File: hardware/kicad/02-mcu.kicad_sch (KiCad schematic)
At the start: 6 parts, among them SW14 BOOT, SW15 RESET, U1 ESP32-S3-N16R8

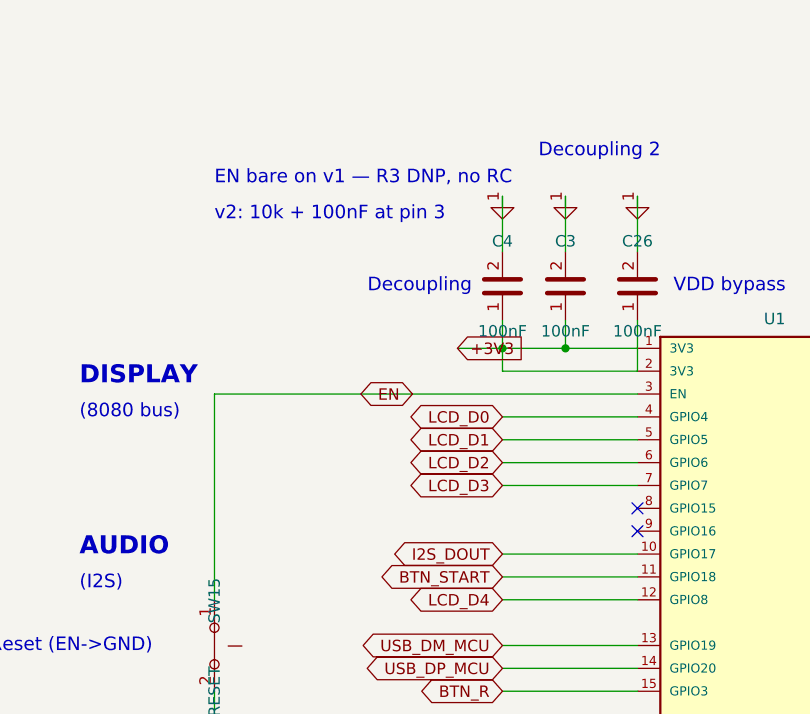
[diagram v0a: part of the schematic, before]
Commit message: feat(hw): EN RC network, fused VBUS input, current-limited backlight — R25 respin trio
Three coordinated design fixes landed together with their full gate,
bench and release integration (work split across two parallel sessions):

- R3 (10k) + C31 (100nF) on EN — the RC the module datasheet p.28
  fig.7 requires (R25-CRIT-1: every board through v4.3.1 shipped
  without it on the strength of a false justification comment).
  EN now solves to the +3V3 rail through the pull-up.
- F1 (PTC resettable fuse 2A 1812, C960026) on the USB input:
  J1 delivers on the new VBUS_IN net and reaches VBUS through F1.
  PWR_FLAG added on the post-fuse rail (J1's power-out pin moved nets).
- R27 (20R 1206) backlight series resistor: LED-A now fed from +5V
  through R27 on the new LED_BLA net (R25-HIGH-1, unbounded current).
  First placement collided with the LCD B.Cu verticals; final position
  (121.7, 45.5) clears the corridor.

Integration completed in this commit:
- verify_polarity: strict expectations for R3/C31/R27/F1, J1 pins moved
  to VBUS_IN, J4.8 backlight expectation moved to LED_BLA — all read
  off the copper.
- vbench corpus: R25-CRIT-1, R10-LOW-7, R25-HIGH-1 flipped from live
  board facts to mutation reinjection (detach R3/C31/R27 must be caught
  by name); R24-HIGH-3 moved to a move_pin drift mutation — the detach
  variant became structurally invisible to the bench once EN gained
  R3/C31 (declared-pad D3 exemption); note records why. usb_cold_boot
  flips its EN assertion exactly as its own text promised; export
  header now derives VB_EN_FLOATING=0; VBUS invariant follows the
  fused chain.
- Gates: R_1206/F_1812 footprints known, F1 value mapping, LED_BLA in
  the Net Explorer section law, schematic caption collisions resolved.
- Release fully synced (gerbers, BOM, CPL, d356, zip, jlcpcb mirror),
  iBOM + schematic SVG/PDF renders + combined PDF regenerated.

Tests: verify-all ALL CHECKS PASSED (incl. polarity 274 checks,
netlist-diff, isolation, e-test on release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
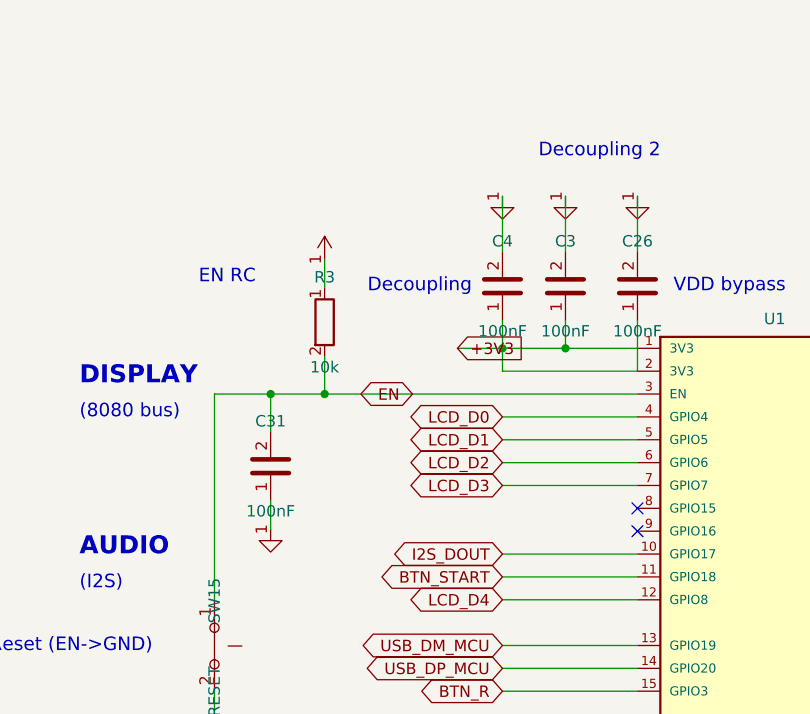
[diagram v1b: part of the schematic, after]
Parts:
- added C26, C3: 100nF, symbol C
- C31: renamed from SW14; value BOOT -> 100nF; symbol SW_Push -> C
- R3: renamed from SW15; value RESET -> 10k; symbol SW_Push -> R
- SW14: renamed from C3; value 100nF -> BOOT; symbol C -> SW_Push
- SW15: renamed from C4; value 100nF -> RESET; symbol C -> SW_Push
- renumbered C26 to C4
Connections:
- net +3V3: now also R3.1, C26.1, C3.1; no longer SW14.1, SW15.1
- net BTN_SELECT: now also SW14.1; no longer C31.1
- net EN: now also C31.2, R3.2, SW15.1; no longer R3.1
- net GND: now also C31.1, C26.2, C3.2; no longer C31.2, R3.2
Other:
- note added: "EN RC"
- note removed: "EN bare on v1 — R3 DNP, no RC"
- note removed: "v2: 10k + 100nF at pin 3"
- moved on the sheet: C4

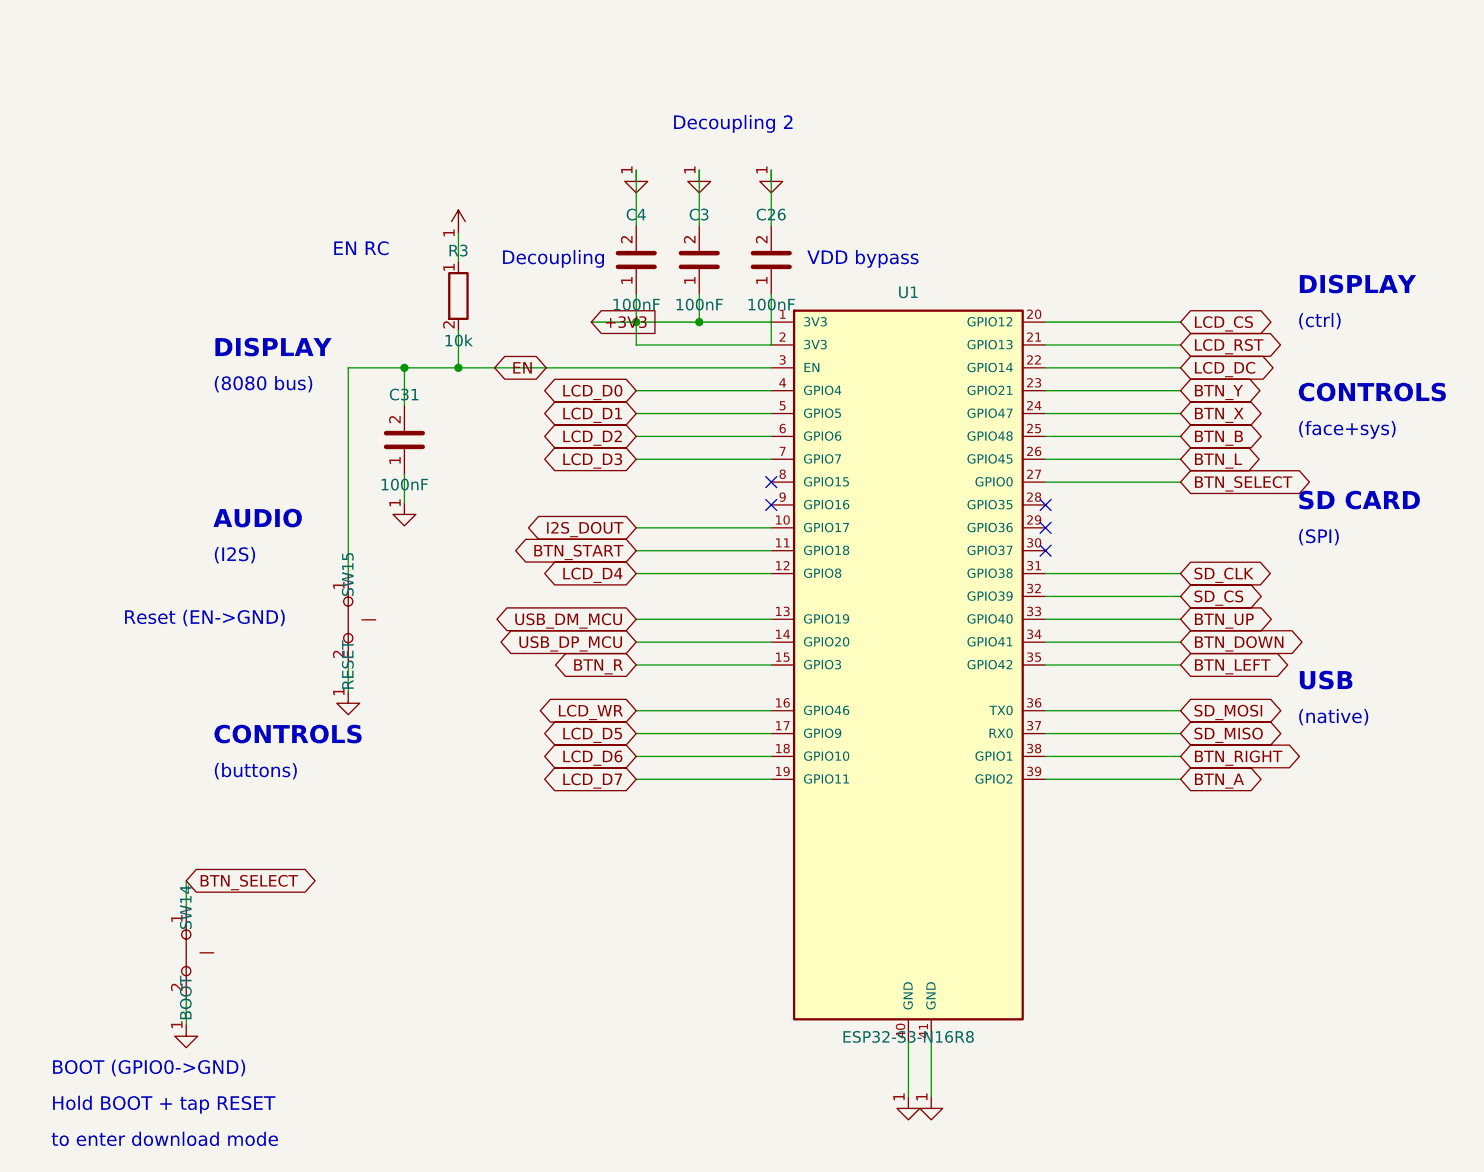
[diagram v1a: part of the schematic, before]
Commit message: feat(containment): layer 6 — ERC warning burn-down, 676 to ZERO, gate at all severities
Three root causes, three fixes in the schematic generator:

- 507 endpoint_off_grid: sheets lay out on a human 1 mm grid while KiCad
  connects on 1.27 mm. snap() in kicad_primitives now grid-snaps every
  connection-bearing coordinate at emission. Snapping is monotonic and
  distributes over the library's grid-multiple pin offsets, so points
  that coincided before still coincide after; zero-length stub wires
  that collapse onto their anchor are dropped.
- The stragglers came from three symbols whose pin connection points
  were themselves off-grid: BAT54C (±5.0 → ±5.08, top 5.0 → 5.08, used
  by D1 and Q1), USBLC6-2SC6 (±10.0 → ±10.16), Speaker (±0.635 →
  ±1.27). Their sheet wiring moved with them in the same commit.
- 169 lib_symbol_issues: bare lib_ids referenced library "" which no
  configuration includes. Symbols are now emu:<name>, resolved by a
  generated hardware/kicad/sym-lib-table + emu.kicad_sym built from the
  same SYMBOLS strings as the embedded caches — cache and library
  cannot disagree by construction.

verify_erc now runs --severity-all against a ZERO baseline: from zero,
any new warning is a regression a specific change introduced. The
website's per-sheet SVGs/PDFs are re-rendered, and the "Download all
sheets" PDF — a one-off hand merge nothing regenerated, stale since the
R25 respin — is now merged by render-schematics.sh from the exported
sheets.

Suite: 85/85 green; netlist_diff vs PCB confirms connectivity unchanged.

Co-Authored-By: Claude Fable 5 <noreply@anthropic.com>
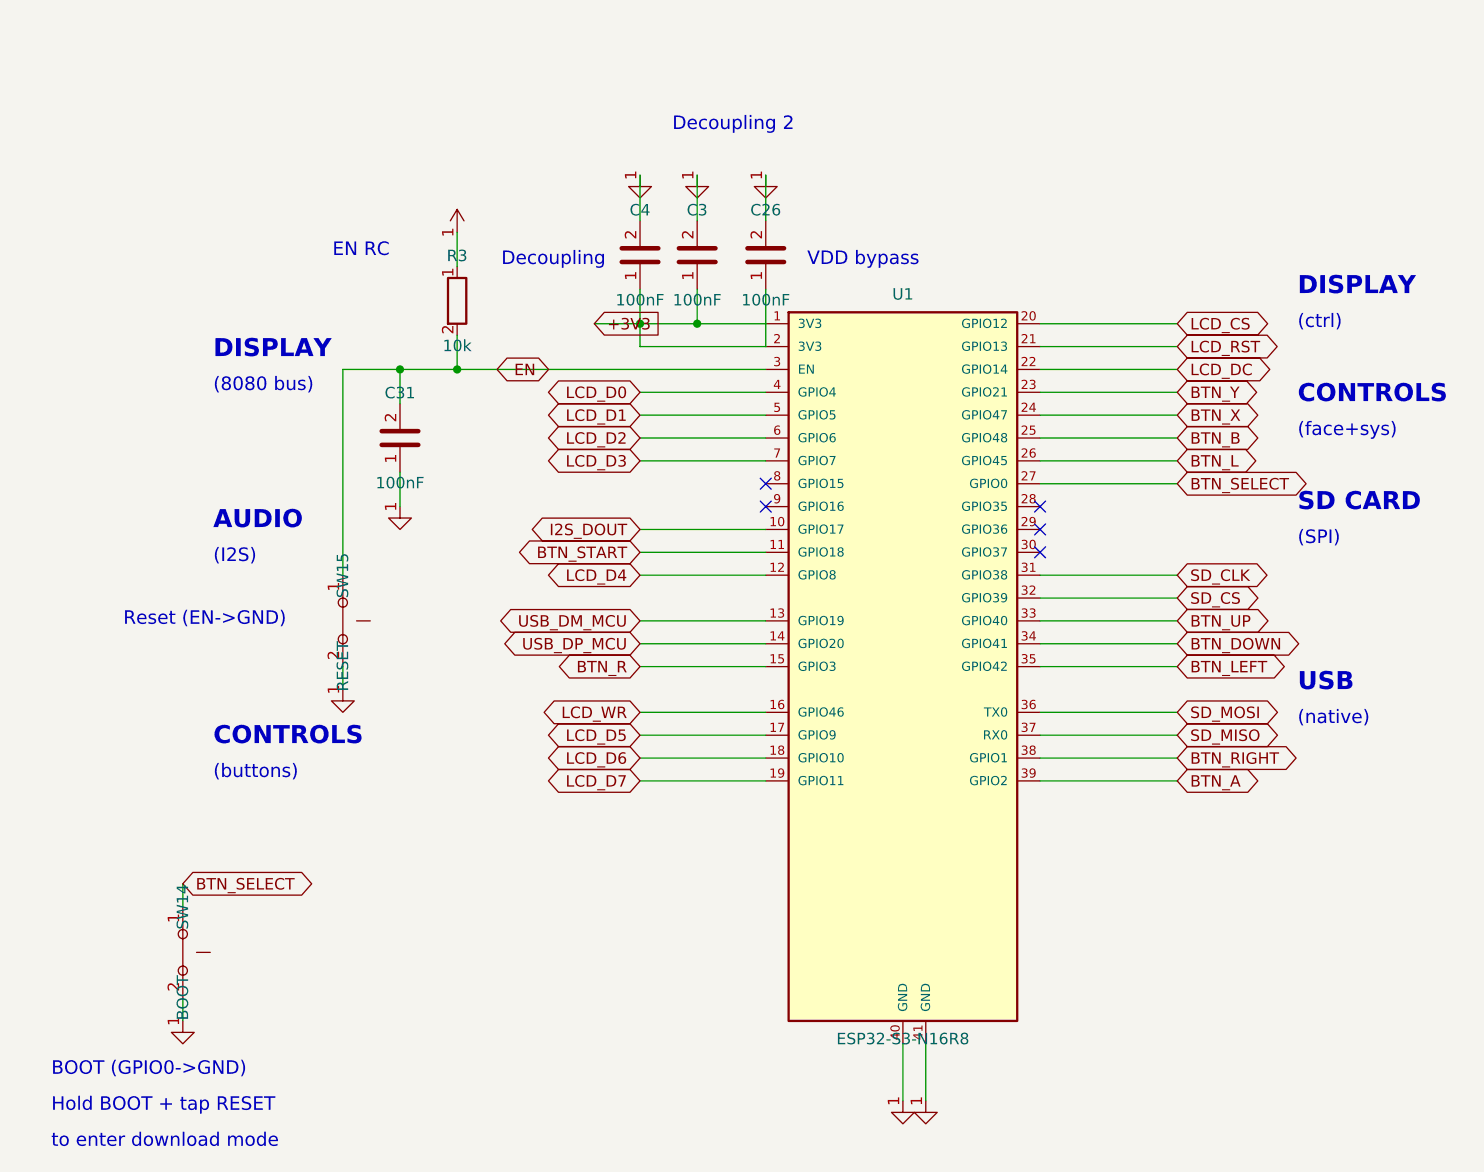
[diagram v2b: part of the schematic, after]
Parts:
- C26, C3, C31, C4: symbol C -> emu:C
- R3: symbol R -> emu:R
- SW14, SW15: symbol SW_Push -> emu:SW_Push
- U1: symbol ESP32-S3-WROOM-1 -> emu:ESP32-S3-WROOM-1
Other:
- moved on the sheet: C26, C3, C31, C4, R3, SW15, U1

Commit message: feat(diag-leds): two-tier diagnostic LED tree — photo-diagnosable rails + firmware heartbeat
Hardware (workstream H): LED3/R28 on VBUS, LED4/R29 on +5V, LED5/R30 on
+3V3 (passive rail indicators), LED6/R31 on LED_HB (GPIO15 heartbeat) —
all C19171391 red 0805 at ~1 mA, grouped TOP-edge bank silk-labelled
VBUS/5V/3V3/HB, DNP in production. Schematic (power + MCU sheets),
placement, routing, BOM/CPL, datasheet_specs, strict polarity-gate
entries read off the copper.

Firmware (workstream F): LED_HB define in board_config.h (GPIO15,
active HIGH: GPIO -> R31 -> anode, cathode to GND), bringup_test
heartbeat — 1 Hz steady = alive, N blinks + pause = subsystem N failed
(2=SD, 3=display, 4=audio, 5=buttons, 6=PSRAM), BRINGUP-LED telemetry.

Docs: diagnostic-leds roadmap + rework page, first-boot procedure,
bring-up protocol (58 checks), short-test page historical banner.

Also: render_pcba.sh mktemp portability (GNU mktemp needs a XXXXXX
template; BSD accepted the bare -t prefix).

Verification: verify-all 93/93 · verify_dfa 9/9 · injection audit 13/13
fault classes caught · release_jlcpcb synced (incl. nested mirror) +
order-manifest + 13 raytraced renders + repo-map.

Replaces WIP commit 26bc2a0.

Co-Authored-By: Claude Fable 5 <noreply@anthropic.com>
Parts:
- added LED6: Red, symbol emu:LED
- added SW15: RESET, symbol emu:SW_Push
- R31: renamed from SW15; value RESET -> 1k; symbol emu:SW_Push -> emu:R
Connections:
- net EN: now also SW15.1; no longer R31.1
- net GND: now also LED6.2 (K), SW15.2; no longer R31.2
- net LED_HB: now reaches U1.8 (GPIO15)
- net LED_HB: now also R31.2
- new net LED6_RA: LED6.1 (A), R31.1
- no-connect marks 5 -> 4
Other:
- note added: "HEARTBEAT LED (GPIO15, DNP in production)"
